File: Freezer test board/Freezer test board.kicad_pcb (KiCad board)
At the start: 4 copper layers, 56 x 65 mm, 13 parts, among them J2 Conn_02x20_Odd_Even, J3 284391-3, J4 284391-3, J5 284391-3, J6 284391-3, J7 284391-3, J8 284391-3, J9 284391-3

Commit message: Reroute GPIO traces on top layer
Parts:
- moved R1 20.5 mm to (96.5, 73.3), turned to -90 degrees
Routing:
- net GPIO24: track 181.4 -> 131.8 mm
- net +3V3: track 162.5 -> 117.4 mm
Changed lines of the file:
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@@
 	(footprint "Resistor_THT:R_Axial_DIN0204_L3.6mm_D1.6mm_P5.08mm_Horizontal"
 		(layer "F.Cu")
-		(at 114.675 63.72 180)
+		(at 96.5 73.26 -90)
 		(descr "Resistor, Axial_DIN0204 series, Axial, Horizontal, pin pitch=5.08mm, 0.167W, length*diameter=3.6*1.6mm^2, http://cdn-reichelt.de/documents/datenblatt/B400/1_4W%23YAG.pdf")
 		(tags "Resistor Axial_DIN0204 series Axial Horizontal pin pitch 5.08mm 0.167W length 3.6mm diameter 1.6mm")
 		(property "Reference" "R1"
-			(at 2.54 -1.92 180)
+			(at 2.54 -1.92 90)
 			(layer "F.SilkS")
 			(effects
@@
 		)
 		(property "Value" "4.7k"
-			(at 2.54 1.92 180)
+			(at 2.54 1.92 90)
 			(layer "F.Fab")
 			(effects
@@
 		)
 		(property "Datasheet" "~"
-			(at 0 0 180)
+			(at 0 0 90)
 			(layer "F.Fab")
 			(hide yes)
@@
 		)
 		(property "Description" "Resistor"
-			(at 0 0 180)
+			(at 0 0 90)
 			(layer "F.Fab")
 			(hide yes)
@@
 		)
 		(fp_line
-			(start 5.08 0)
-			(end 4.34 0)
+			(start 0 0)
+			(end 0.74 0)
 			(stroke
 				(width 0.1)
@@
 		)
 		(fp_line
-			(start 0 0)
-			(end 0.74 0)
+			(start 5.08 0)
+			(end 4.34 0)
 			(stroke
 				(width 0.1)
@@
 		)
 		(fp_text user "${REFERENCE}"
-			(at 2.54 0 180)
+			(at 2.54 0 90)
 			(layer "F.Fab")
 			(effects
@@
 		)
 		(pad "1" thru_hole circle
-			(at 0 0 180)
+			(at 0 0 270)
 			(size 1.4 1.4)
 			(drill 0.7)
@@
 		)
 		(pad "2" thru_hole circle
-			(at 5.08 0 180)
+			(at 5.08 0 270)
 			(size 1.4 1.4)
 			(drill 0.7)
@@
 	)
 	(segment
-		(start 87.71 93.6)
-		(end 89.05 92.26)
-		(width 0.2)
-		(layer "F.Cu")
-		(net 2)
-	)
-	(segment
-		(start 92.3 72.22)
-		(end 100.8 63.72)
-		(width 0.2)
-		(layer "F.Cu")
-		(net 2)
-	)
-	(segment
-		(start 92.3 90.63776)
-		(end 92.3 72.22)
-		(width 0.2)
-		(layer "F.Cu")
-		(net 2)
-	)
-	(segment
-		(start 89.05 92.26)
-		(end 90.67776 92.26)
-		(width 0.2)
-		(layer "F.Cu")
-		(net 2)
-	)
-	(segment
-		(start 100.8 63.72)
-		(end 109.595 63.72)
-		(width 0.2)
-		(layer "F.Cu")
-		(net 2)
-	)
-	(segment
-		(start 90.67776 92.26)
-		(end 92.3 90.63776)
-		(width 0.2)
-		(layer "F.Cu")
-		(net 2)
-	)
-	(segment
 		(start 104.5 92.449)
 		(end 88.861 92.449)
@@
 	)
 	(segment
-		(start 131.58 80.97)
-		(end 131.58 69.08)
-		(width 0.2)
-		(layer "F.Cu")
-		(net 36)
-	)
-	(segment
-		(start 134.74 48.24)
-		(end 131.58 48.24)
-		(width 0.2)
+		(start 101 96.5)
+		(end 101 94)
+		(width 0.3)
 		(layer "F.Cu")
 		(net 36)
 	)
 	(segment
-		(start 136 73.5)
-		(end 131.58 69.08)
-		(width 0.2)
+		(start 131.58 80.97)
+		(end 131.58 73.5)
+		(width 0.3)
 		(layer "F.Cu")
 		(net 36)
 	)
 	(segment
-		(start 114.675 63.72)
-		(end 114.675 62.245)
-		(width 0.2)
+		(start 113 89.74)
+		(end 119.76 89.74)
+		(width 0.3)
 		(layer "F.Cu")
 		(net 36)
 	)
 	(segment
-		(start 136 61.5)
-		(end 135.5 62)
-		(width 0.2)
+		(start 90.25 73.28)
+		(end 96.48 73.28)
+		(width 0.3)
 		(layer "F.Cu")
 		(net 36)
 	)
 	(segment
-		(start 114.675 62.245)
-		(end 114.63 62.2)
-		(width 0.2)
+		(start 96.48 73.28)
+		(end 96.5 73.26)
+		(width 0.3)
 		(layer "F.Cu")
 		(net 36)
 	)
 	(segment
-		(start 136 49.5)
-		(end 134.74 48.24)
-		(width 0.2)
+		(start 131.58 85.5)
+		(end 131.58 80.97)
+		(width 0.3)
 		(layer "F.Cu")
 		(net 36)
 	)
 	(segment
-		(start 114.675 49.325)
-		(end 114.675 63.72)
-		(width 0.2)
+		(start 131.58 49.5)
+		(end 131.58 61.5)
+		(width 0.3)
 		(layer "F.Cu")
 		(net 36)
 	)
 	(segment
-		(start 115.76 48.24)
-		(end 114.675 49.325)
-		(width 0.2)
+		(start 113 96.5)
+		(end 113 89.74)
+		(width 0.3)
 		(layer "F.Cu")
 		(net 36)
 	)
 	(segment
-		(start 131.58 57.08)
-		(end 131.58 48.24)
-		(width 0.2)
+		(start 136 61.5)
+		(end 135.5 62)
+		(width 0.3)
 		(layer "F.Cu")
 		(net 36)
 	)
 	(segment
-		(start 101.33 62.2)
-		(end 90.25 73.28)
-		(width 0.2)
+		(start 125 96.5)
+		(end 125 89.74)
+		(width 0.3)
 		(layer "F.Cu")
 		(net 36)
 	)
 	(segment
-		(start 131.58 89.92)
-		(end 131.58 89.74)
-		(width 0.2)
+		(start 136 49.5)
+		(end 131.58 49.5)
+		(width 0.3)
 		(layer "F.Cu")
 		(net 36)
 	)
 	(segment
-		(start 107.76 89.74)
-		(end 119.76 89.74)
-		(width 0.2)
+		(start 105.26 82.02)
+		(end 105.26 89.74)
+		(width 0.3)
 		(layer "F.Cu")
 		(net 36)
 	)
 	(segment
-		(start 113.155 62.2)
-		(end 101.33 62.2)
-		(width 0.2)
+		(start 136 61.5)
+		(end 131.58 61.5)
+		(width 0.3)
 		(layer "F.Cu")
 		(net 36)
 	)
 	(segment
-		(start 131.58 69.08)
-		(end 131.58 57.08)
-		(width 0.2)
+		(start 131.58 87.16)
+		(end 131.58 85.5)
+		(width 0.3)
 		(layer "F.Cu")
 		(net 36)
 	)
 	(segment
-		(start 119.76 89.74)
-		(end 131.58 89.74)
-		(width 0.2)
+		(start 129 89.74)
+		(end 131.58 87.16)
+		(width 0.3)
 		(layer "F.Cu")
 		(net 36)
 	)
 	(segment
-		(start 101 96.5)
-		(end 107.76 89.74)
-		(width 0.2)
+		(start 131.58 69.08)
+		(end 131.58 61.5)
+		(width 0.3)
 		(layer "F.Cu")
 		(net 36)
 	)
 	(segment
-		(start 131.58 48.24)
-		(end 115.76 48.24)
-		(width 0.2)
+		(start 136 73.5)
+		(end 131.58 73.5)
+		(width 0.3)
 		(layer "F.Cu")
 		(net 36)
 	)
 	(segment
-		(start 131.58 89.74)
-		(end 131.58 80.97)
-		(width 0.2)
+		(start 125 89.74)
+		(end 129 89.74)
+		(width 0.3)
 		(layer "F.Cu")
 		(net 36)
 	)
 	(segment
-		(start 114.675 63.72)
-		(end 113.155 62.2)
-		(width 0.2)
+		(start 119.76 89.74)
+		(end 125 89.74)
+		(width 0.3)
 		(layer "F.Cu")
 		(net 36)
@@
 	(segment
 		(start 136 85.5)
-		(end 131.58 81.08)
-		(width 0.2)
+		(end 131.58 85.5)
+		(width 0.3)
 		(layer "F.Cu")
 		(net 36)
 	)
 	(segment
-		(start 125 96.5)
-		(end 131.58 89.92)
-		(width 0.2)
+		(start 131.58 73.5)
+		(end 131.58 69.08)
+		(width 0.3)
 		(layer "F.Cu")
 		(net 36)
 	)
 	(segment
-		(start 136 61.5)
-		(end 131.58 57.08)
-		(width 0.2)
+		(start 101 94)
+		(end 105.26 89.74)
+		(width 0.3)
 		(layer "F.Cu")
 		(net 36)
 	)
 	(segment
-		(start 131.58 81.08)
-		(end 131.58 80.97)
-		(width 0.2)
+		(start 96.5 73.26)
+		(end 105.26 82.02)
+		(width 0.3)
 		(layer "F.Cu")
 		(net 36)
 	)
 	(segment
-		(start 113 96.5)
-		(end 119.76 89.74)
-		(width 0.2)
+		(start 105.26 89.74)
+		(end 113 89.74)
+		(width 0.3)
 		(layer "F.Cu")
 		(net 36)

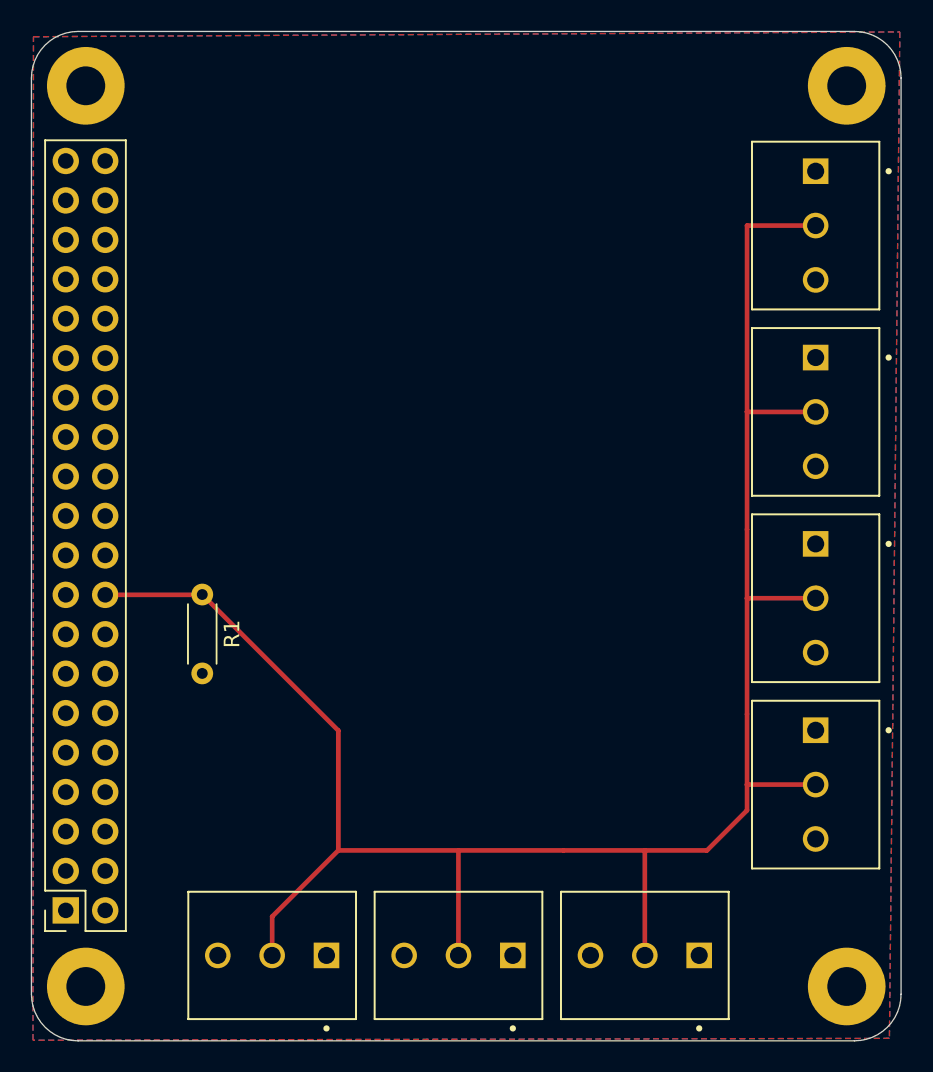
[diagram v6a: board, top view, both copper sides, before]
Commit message: fixed?
reverted to the Tri's previous push and then re did the signal tracks, re organized the resistors and terminal blocks. Other than everything is the exact same
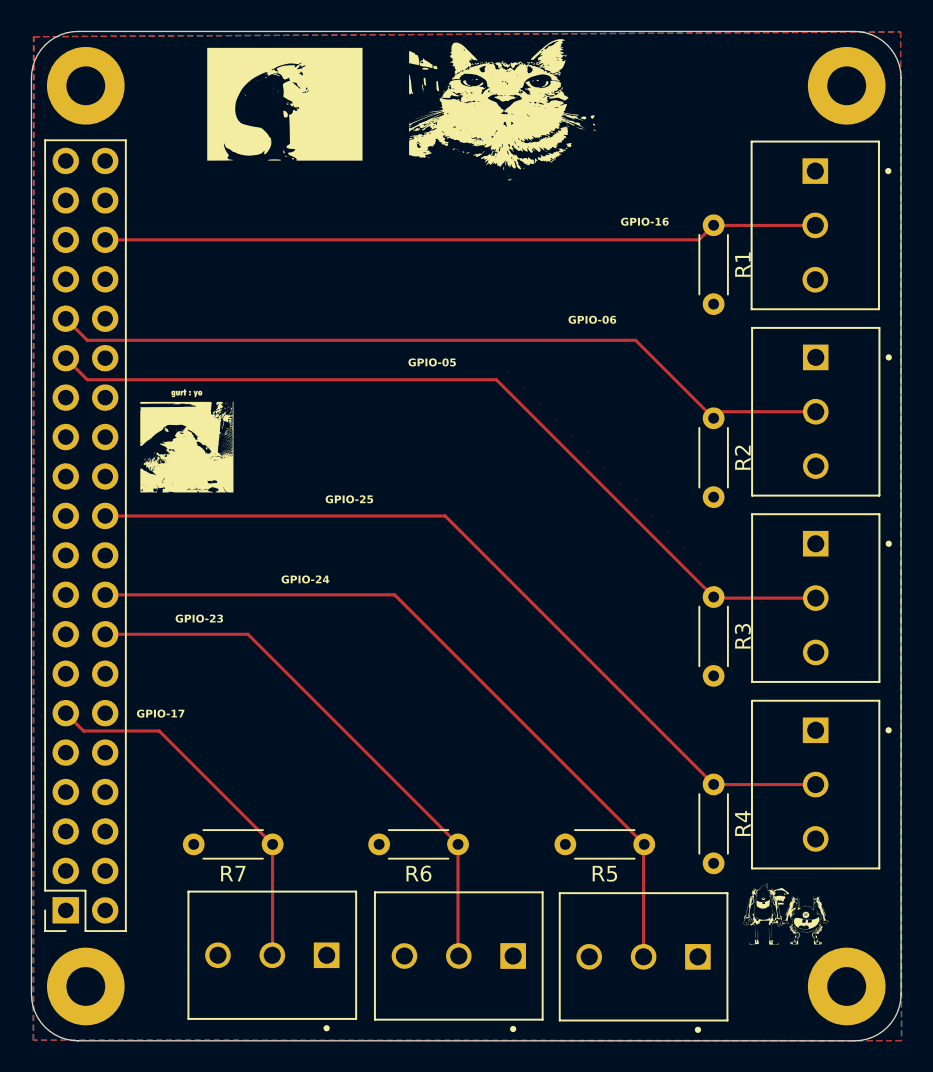
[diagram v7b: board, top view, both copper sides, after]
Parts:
- added G***: LOGO, LOGO, F.Cu at (134.1, 93.8)
- added G***: LOGO, LOGO, F.Cu at (101.8, 41.7)
- added G***: LOGO, LOGO, F.Cu at (95.5, 63.2)
- added G***: LOGO, LOGO, F.Cu at (115.8, 41.4)
- added G***: LOGO, LOGO, B.Cu at (120.6, 71.3)
- added R2: 4.7k, Resistor_THT:R_Axial_DIN0204_L3.6mm_D1.6mm_P5.08mm_Horizontal, F.Cu at (129.4, 61.9)
- added R3: 4.7k, Resistor_THT:R_Axial_DIN0204_L3.6mm_D1.6mm_P5.08mm_Horizontal, F.Cu at (129.4, 73.4)
- added R4: 4.7k, Resistor_THT:R_Axial_DIN0204_L3.6mm_D1.6mm_P5.08mm_Horizontal, F.Cu at (129.4, 85.5)
- added R5: 4.7k, Resistor_THT:R_Axial_DIN0204_L3.6mm_D1.6mm_P5.08mm_Horizontal, F.Cu at (125.0, 89.3)
- added R6: 4.7k, Resistor_THT:R_Axial_DIN0204_L3.6mm_D1.6mm_P5.08mm_Horizontal, F.Cu at (113.0, 89.3)
- added R7: 4.7k, Resistor_THT:R_Axial_DIN0204_L3.6mm_D1.6mm_P5.08mm_Horizontal, F.Cu at (101.0, 89.3)
- moved J3 58.6 mm to (136.0, 49.5), turned to -90 degrees
- moved J9 58.6 mm to (101.0, 96.5), turned to 180 degrees
- moved J8 41.9 mm to (113.0, 96.5), turned to 180 degrees
- moved J4 41.9 mm to (136.0, 61.5), turned to -90 degrees
- moved R1 40.6 mm to (129.4, 49.5)
- moved J7 25.6 mm to (124.9, 96.6), turned to 180 degrees
- moved J5 25.5 mm to (136.0, 73.5), turned to -90 degrees
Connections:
- J2 pad 11: unconnected-(J2-Pin_11-Pad11) -> GPIO17
- J2 pad 16: unconnected-(J2-Pin_16-Pad16) -> GPIO23
- J2 pad 22: unconnected-(J2-Pin_22-Pad22) -> GPIO25
- J2 pad 29: unconnected-(J2-Pin_29-Pad29) -> GPIO5
- J2 pad 31: unconnected-(J2-Pin_31-Pad31) -> GPIO6
- J2 pad 36: unconnected-(J2-Pin_36-Pad36) -> GPIO16
- J3 pad 2: GPIO24 -> GPIO16
- J4 pad 2: GPIO24 -> GPIO6
- J5 pad 2: GPIO24 -> GPIO5
- J6 pad 2: GPIO24 -> GPIO25
- J8 pad 2: GPIO24 -> GPIO23
- J9 pad 2: GPIO24 -> GPIO17
- R1 pad 1: GPIO24 -> GPIO16
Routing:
- net GND: track 174.1 -> 0.00 mm
- net +3V3: track 117.4 -> 0.00 mm
- net GPIO24: track 131.8 -> 48.6 mm
- net GPIO5: track 0.00 -> 54.7 mm
- net GPIO25: track 0.00 -> 52.9 mm
- net GPIO6: track 0.00 -> 51.8 mm
- net GPIO16: track 0.00 -> 46.1 mm
- net GPIO23: track 0.00 -> 35.5 mm
- net GPIO17: track 0.00 -> 24.0 mm
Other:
- board text added: "Freezer Test PCB"
- board text added: "GPIO-05"
- board text added: "GPIO-06"
- board text added: "GPIO-16"
- board text added: "GPIO-17"
- board text added: "GPIO-23"
- board text added: "GPIO-24"
- board text added: "GPIO-25"
- board text added: "Made By Jason Suarez"
- board text added: "Made with the Power of {dblquote}What are we doing Mannn{dblquote}-Tri"
- board text added: "im a dandelion twin"

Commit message: Finial Touches
put what specific resistors are being used in the comments. Made the finial touches and re traced the resistors and spaced them further from the terminal blocks
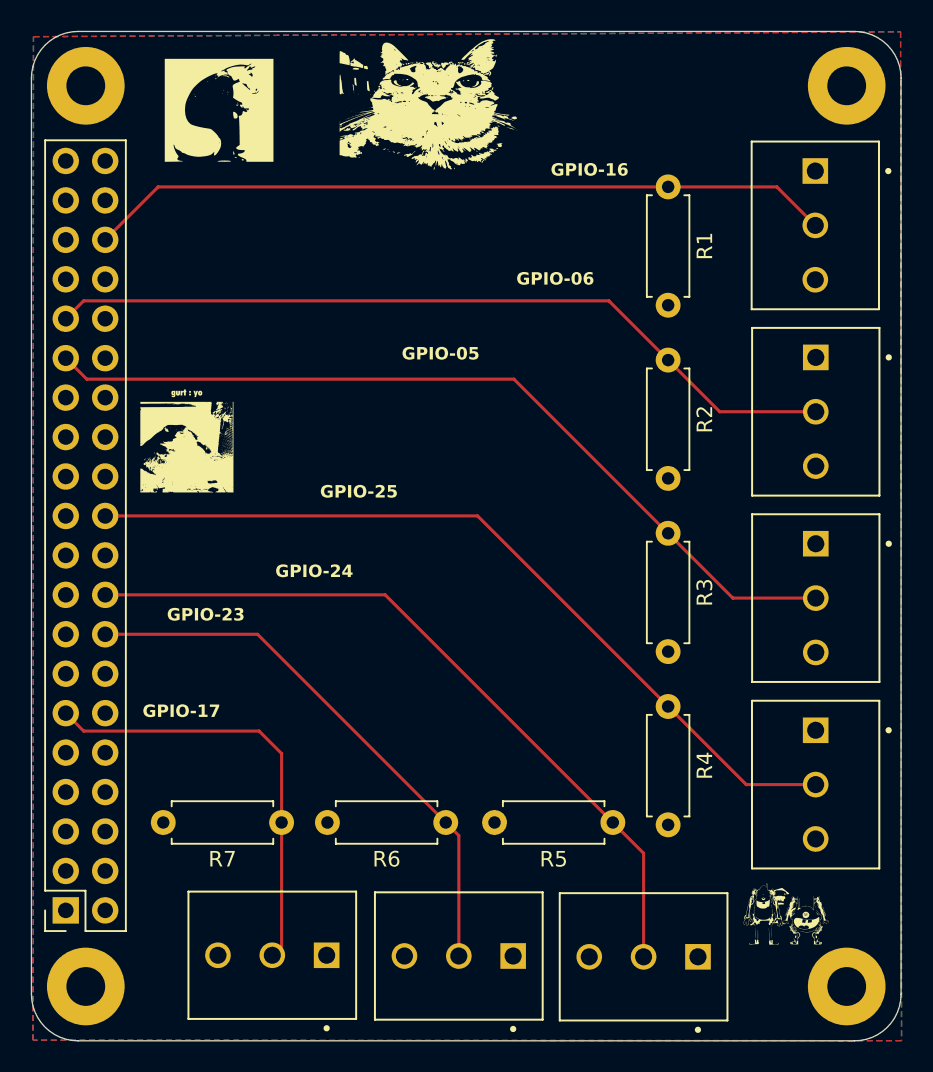
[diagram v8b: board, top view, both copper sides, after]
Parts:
- R1, R2, R3, R4, R5, R6, R7: footprint Resistor_THT:R_Axial_DIN0204_L3.6mm_D1.6mm_P5.08mm_Horizontal -> Resistor_THT:R_Axial_DIN0207_L6.3mm_D2.5mm_P7.62mm_Horizontal
- moved R4 5.81 mm to (126.5, 80.5)
- moved G*** 5.48 mm to (115.1, 71.3)
- moved R3 5.04 mm to (126.5, 69.3)
- moved R2 4.76 mm to (126.5, 58.2)
- moved G*** 4.47 mm to (111.3, 41.4)
- moved R1 3.83 mm to (126.5, 47.0)
- moved G*** 3.24 mm to (98.6, 41.8)
- moved R5 2.46 mm to (122.9, 87.9)
- moved R6 1.62 mm to (112.2, 87.9)
- moved R7 1.52 mm to (101.6, 87.9)
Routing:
- net GPIO17: track 24.0 -> 28.2 mm
- net GPIO16: track 46.1 -> 48.2 mm
